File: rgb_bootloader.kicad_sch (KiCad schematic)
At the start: 12 parts, among them J5 USB-C fingers, J6 FFC programming interface, U2 ATtiny84A-CC

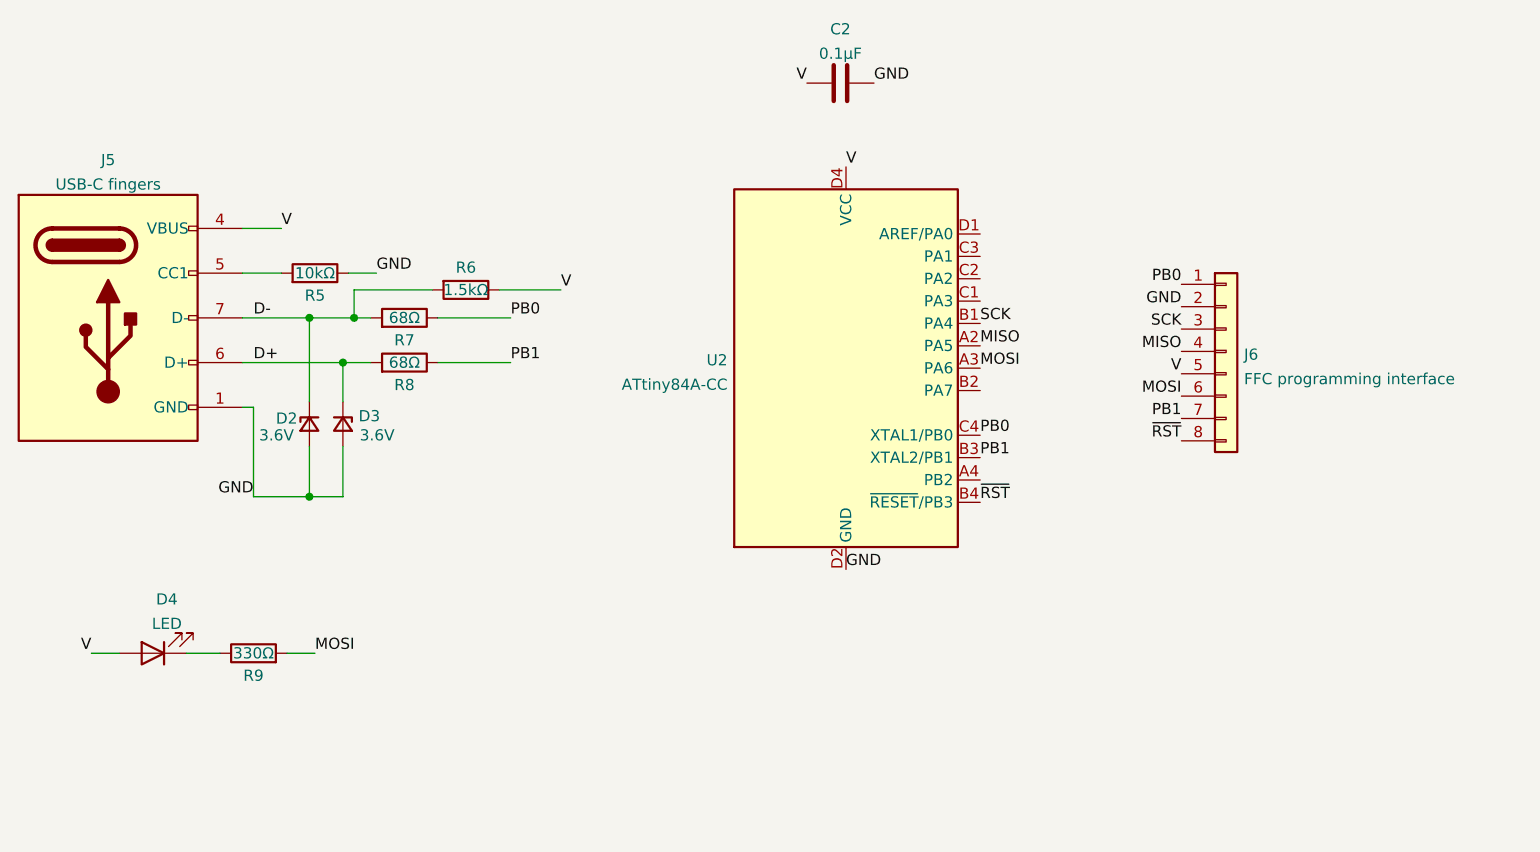
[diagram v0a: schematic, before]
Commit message: Finished routing Demo 2, added Demo 4, updated readme with newer findings
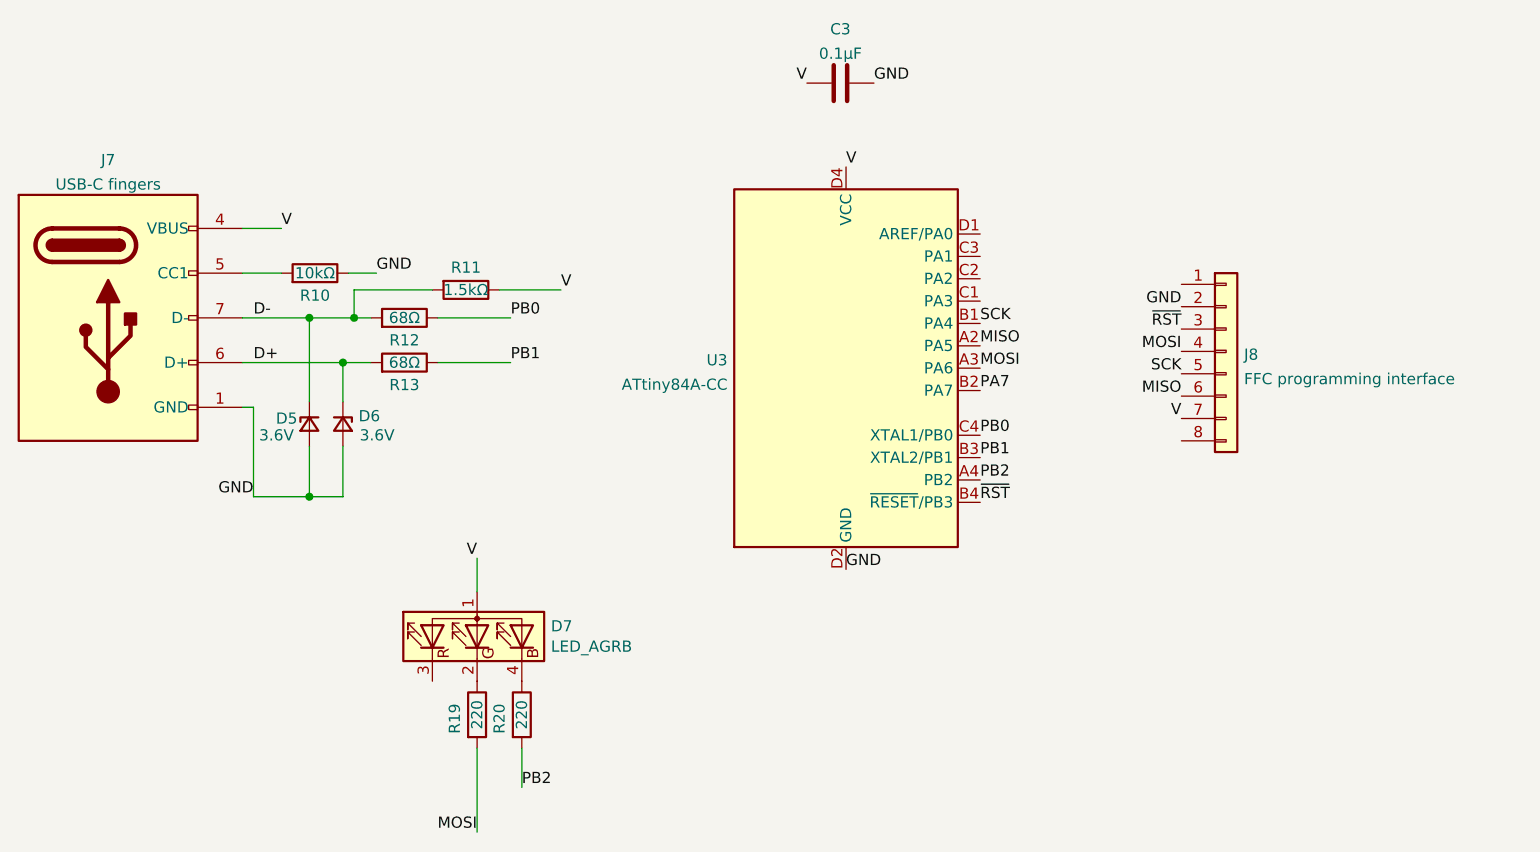
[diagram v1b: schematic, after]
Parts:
- removed C2: 0.1μF, Capacitor_SMD:C_0402_1005Metric, symbol Device:C
- removed D2, D3: 3.6V, Diode_SMD:D_0402_1005Metric, symbol Device:D_Zener_Small
- removed D4: LED, LED_SMD:LED_0402_1005Metric, symbol Device:LED
- removed J5: USB-C fingers, USB-C_PCB_experiments:usb-c-one-sided, symbol USB-C_PCB_experiments:PCB_USB_C_Receptacle
- removed J6: FFC programming interface, USB-C_PCB_experiments:FFC-08, symbol Connector_Generic:Conn_01x08
- removed R5: 10kΩ, Resistor_SMD:R_0402_1005Metric, symbol Device:R
- removed R6: 1.5kΩ, Resistor_SMD:R_0402_1005Metric, symbol Device:R
- removed R7, R8: 68Ω, Resistor_SMD:R_0402_1005Metric, symbol Device:R
- removed R9: 330Ω, Resistor_SMD:R_0402_1005Metric, symbol Device:R
- removed U2: ATtiny84A-CC, Package_BGA:UFBGA-15_3.0x3.0mm_Layout4x4_P0.65mm, symbol MCU_Microchip_ATtiny:ATtiny84A-CC
- added C3: 0.1μF, Capacitor_SMD:C_0402_1005Metric, symbol Device:C
- added D5, D6: 3.6V, Diode_SMD:D_0402_1005Metric, symbol Device:D_Zener_Small
- added D7: LED_AGRB, USB-C_PCB_experiments:LED_everlight_EASV2713RGBA1, symbol Device:LED_AGRB
- added J7: USB-C fingers, USB-C_PCB_experiments:usb-c-one-sided, symbol USB-C_PCB_experiments:PCB_USB_C_Receptacle
- added J8: FFC programming interface, USB-C_PCB_experiments:FFC-08, symbol Connector_Generic:Conn_01x08
- added R10: 10kΩ, Resistor_SMD:R_0402_1005Metric, symbol Device:R
- added R11: 1.5kΩ, Resistor_SMD:R_0402_1005Metric, symbol Device:R
- added R12, R13: 68Ω, Resistor_SMD:R_0402_1005Metric, symbol Device:R
- added R19, R20: 220, Resistor_SMD:R_0201_0603Metric, symbol Device:R
- added U3: ATtiny84A-CC, Package_BGA:UFBGA-15_3.0x3.0mm_Layout4x4_P0.65mm, symbol MCU_Microchip_ATtiny:ATtiny84A-CC
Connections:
- net D+: now also D6.1 (K), J7.6 (D+), R13.2
- net D-: now also D5.1 (K), J7.7 (D-), R11.2, R12.2
- net GND: now also C3.1, D5.2 (A), D6.2 (A), J7.1 (GND), J7.12 (GND), J8.2 (Pin_2), R10.1, U3.D2 (GND), U3.D3 (GND)
- net MISO: now also J8.6 (Pin_6), U3.A2 (PA5)
- net MOSI: now also J8.4 (Pin_4), R19.2, U3.A3 (PA6)
- net PB0: now also R12.1, U3.C4 (XTAL1/PB0)
- net PB1: now also R13.1, U3.B3 (XTAL2/PB1)
- net SCK: now also J8.5 (Pin_5), U3.B1 (PA4)
- net V: now also C3.2, D7.1 (A), J7.4 (VBUS), J7.9 (VBUS), J8.7 (Pin_7), R11.1, U3.D4 (VCC)
- net ~{RST}: now also J8.3 (Pin_3), U3.B4 (~{RESET}/PB3)
- new net: D7.4 (BK), R20.1
- new net: J7.5 (CC1), R10.2
- new net: D7.2 (GK), R19.1
- new net PA7: U3.B2 (PA7)
- new net PB2: R20.2, U3.A4 (PB2)
